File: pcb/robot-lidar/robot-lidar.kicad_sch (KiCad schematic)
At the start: 50 parts, among them J10 Conn_01x18, J2 YLIDAR X4, J3 Jack-DC, J5 Conn_01x02, J5 Conn_02x03_Odd_Even, J6 Conn_01x02, J7 Conn_01x02, J7 Conn_ARM_SWD_TagConnect_TC2030, J8 Conn_01x02, J9 Conn_01x18, SW1 SW_SPST, U1 STM32F429VETx, U2 LM317-3.3_SOT-223, U2 MPU-6050, U4 MX1508, U5 MX1508, Y1 Crystal

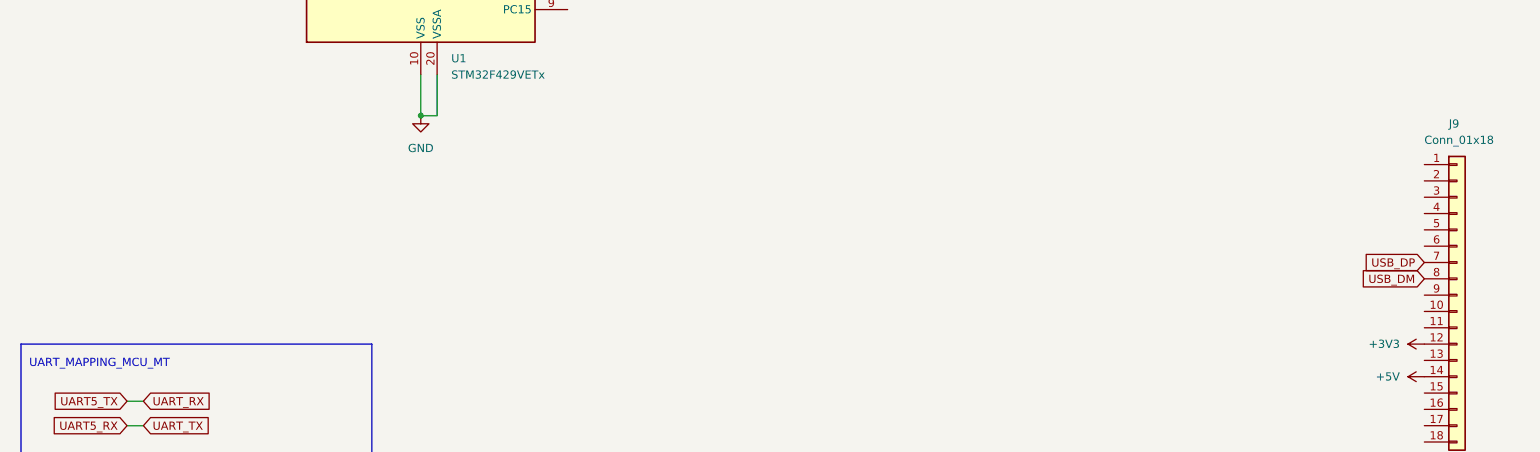
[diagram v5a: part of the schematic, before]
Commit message: add usb a connector
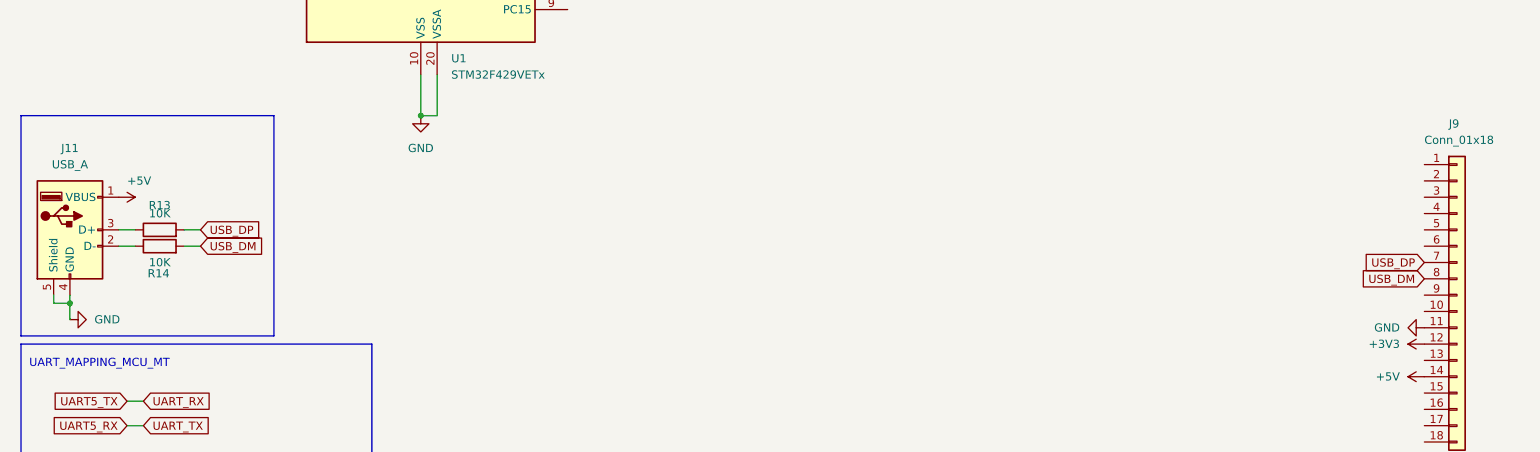
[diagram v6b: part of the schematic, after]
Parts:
- added J11: USB_A, symbol Connector:USB_A
- added R13, R14: 10K, Resistor_SMD:R_0603_1608Metric, symbol Device:R
- J10, J9: footprint (none) -> Connector_PinHeader_2.54mm:PinHeader_1x18_P2.54mm_Vertical
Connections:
- net +5V: now also J11.1 (VBUS)
- net GND: now also J9.11 (Pin_11), J11.4 (GND), J11.5 (Shield)
- net USB_DM: now also R14.2
- net USB_DP: now also R13.2
- new net: J11.3 (D+), R13.1
- new net: J11.2 (D-), R14.1
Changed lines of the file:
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@@
   (junction (at 246.38 106.68) (diameter 0) (color 0 0 0 0)
   )
+  (junction (at 22.86 219.71) (diameter 0) (color 0 0 0 0)
+  )
   (junction (at 246.38 59.69) (diameter 0) (color 0 0 0 0)
   )
@@
     (stroke (width 0) (type default))
   )
+  (wire (pts (xy 22.86 219.71) (xy 22.86 222.25))
+    (stroke (width 0) (type default))
+  )
   (wire (pts (xy 124.46 144.78) (xy 121.92 144.78))
     (stroke (width 0) (type default))
@@
     (stroke (width 0) (type default))
   )
+  (wire (pts (xy 30.48 208.28) (xy 33.02 208.28))
+    (stroke (width 0) (type default))
+  )
   (wire (pts (xy 265.43 151.13) (xy 265.43 157.48))
     (stroke (width 0) (type default))
@@
     (stroke (width 0) (type default))
   )
+  (wire (pts (xy 22.86 218.44) (xy 22.86 219.71))
+    (stroke (width 0) (type default))
+  )
   (wire (pts (xy 80.01 21.59) (xy 80.01 41.91))
     (stroke (width 0) (type default))
@@
     (stroke (width 0) (type default))
   )
+  (wire (pts (xy 40.64 208.28) (xy 43.18 208.28))
+    (stroke (width 0) (type default))
+  )
   (wire (pts (xy 121.92 138.43) (xy 121.92 144.78))
     (stroke (width 0) (type default))
@@
     (stroke (width 0) (type default))
   )
+  (wire (pts (xy 40.64 210.82) (xy 43.18 210.82))
+    (stroke (width 0) (type default))
+  )
   (wire (pts (xy 248.92 46.99) (xy 248.92 50.8))
     (stroke (width 0) (type default))
@@
     (stroke (width 0) (type default))
   )
+  (wire (pts (xy 20.32 219.71) (xy 22.86 219.71))
+    (stroke (width 0) (type default))
+  )
   (wire (pts (xy 35.56 33.02) (xy 43.18 33.02))
     (stroke (width 0) (type default))
@@
     (stroke (width 0) (type default))
   )
+  (wire (pts (xy 20.32 218.44) (xy 20.32 219.71))
+    (stroke (width 0) (type default))
+  )
   (polyline (pts (xy 321.31 41.91) (xy 358.14 41.91))
     (stroke (width 0) (type default))
@@
     (stroke (width 0) (type default))
   )
+  (wire (pts (xy 30.48 210.82) (xy 33.02 210.82))
+    (stroke (width 0) (type default))
+  )
   (wire (pts (xy 392.43 133.35) (xy 392.43 137.16))
     (stroke (width 0) (type default))
@@
     (stroke (width 0) (type default))
   )
+  (rectangle (start 15.24 190.5) (end 54.61 224.79)
+    (stroke (width 0) (type default))
+    (fill (type none))
+  )
   (rectangle (start 72.39 247.65) (end 132.08 280.67)
     (stroke (width 0) (type default))
@@
     )
   )
+  (global_label "USB_DM" (shape input) (at 43.18 210.82 0) (fields_autoplaced)
+    (effects (font (size 1.27 1.27)) (justify left))
+    (property "Intersheetrefs" "${INTERSHEET_REFS}" (at 53.6642 210.82 0)
+      (effects (font (size 1.27 1.27)) (justify left) hide)
+    )
+  )
   (global_label "M_EN" (shape input) (at 382.27 38.1 180) (fields_autoplaced)
     (effects (font (size 1.27 1.27)) (justify right))
@@
     )
   )
+  (global_label "USB_DP" (shape input) (at 43.18 208.28 0) (fields_autoplaced)
+    (effects (font (size 1.27 1.27)) (justify left))
+    (property "Intersheetrefs" "${INTERSHEET_REFS}" (at 53.4828 208.28 0)
+      (effects (font (size 1.27 1.27)) (justify left) hide)
+    )
+  )
   (global_label "MOTOR_1_B" (shape input) (at 100.33 128.27 0) (fields_autoplaced)
     (effects (font (size 1.27 1.27)) (justify left))
@@
       (effects (font (size 1.27 1.27)))
     )
-    (property "Footprint" "" (at 262.89 220.98 0)
+    (property "Footprint" "Connector_PinHeader_2.54mm:PinHeader_1x18_P2.54mm_Vertical" (at 262.89 220.98 0)
       (effects (font (size 1.27 1.27)) hide)
     )
@@
     )
   )
+  (symbol (lib_id "power:+5V") (at 30.48 203.2 270) (unit 1)
+    (in_bom yes) (on_board yes) (dnp no)
+    (property "Reference" "#PWR037" (at 26.67 203.2 0)
+      (effects (font (size 1.27 1.27)) hide)
+    )
+    (property "Value" "+5V" (at 31.75 200.66 90)
+      (effects (font (size 1.27 1.27)) (justify left))
+    )
+    (property "Footprint" "" (at 30.48 203.2 0)
+      (effects (font (size 1.27 1.27)) hide)
+    )
+    (property "Datasheet" "" (at 30.48 203.2 0)
+      (effects (font (size 1.27 1.27)) hide)
+    )
+    (pin "1")
+    (instances
+      (project "robot-lidar"
+        (path "/cb10bbf7-c2c1-4a0d-8947-ad707931d83b"
+          (reference "#PWR037") (unit 1)
+        )
+      )
+    )
+  )
   (symbol (lib_id "Device:C") (at 35.56 26.67 0) (unit 1)
     (in_bom yes) (on_board yes) (dnp no)
@@
     )
   )
+  (symbol (lib_id "Device:R") (at 36.83 208.28 90) (unit 1)
+    (in_bom yes) (on_board yes) (dnp no)
+    (property "Reference" "R13" (at 36.83 204.47 90)
+      (effects (font (size 1.27 1.27)))
+    )
+    (property "Value" "10K" (at 36.83 205.74 90)
+      (effects (font (size 1.27 1.27)))
+    )
+    (property "Footprint" "Resistor_SMD:R_0603_1608Metric" (at 36.83 210.058 90)
+      (effects (font (size 1.27 1.27)) hide)
+    )
+    (property "Datasheet" "~" (at 36.83 208.28 0)
+      (effects (font (size 1.27 1.27)) hide)
+    )
+    (pin "1")
+    (pin "2")
+    (instances
+      (project "robot-lidar"
+        (path "/cb10bbf7-c2c1-4a0d-8947-ad707931d83b"
+          (reference "R13") (unit 1)
+        )
+      )
+      (project "servo_control"
+        (path "/dcee87eb-58b7-46fe-9143-b216c98d2b37"
+          (reference "R15") (unit 1)
+        )
+      )
+    )
+  )
   (symbol (lib_id "Device:C") (at 66.04 26.67 0) (unit 1)
     (in_bom yes) (on_board yes) (dnp no)
@@
     )
   )
+  (symbol (lib_id "power:GND") (at 233.68 223.52 270) (unit 1)
+    (in_bom yes) (on_board yes) (dnp no) (fields_autoplaced)
+    (property "Reference" "#PWR036" (at 227.33 223.52 0)
+      (effects (font (size 1.27 1.27)) hide)
+    )
+    (property "Value" "GND" (at 229.87 223.52 90)
+      (effects (font (size 1.27 1.27)) (justify right))
+    )
+    (property "Footprint" "" (at 233.68 223.52 0)
+      (effects (font (size 1.27 1.27)) hide)
+    )
+    (property "Datasheet" "" (at 233.68 223.52 0)
+      (effects (font (size 1.27 1.27)) hide)
+    )
+    (pin "1")
+    (instances
+      (project "robot-lidar"
+        (path "/cb10bbf7-c2c1-4a0d-8947-ad707931d83b"
+          (reference "#PWR036") (unit 1)
+        )
+      )
+    )
+  )
   (symbol (lib_id "Device:C") (at 392.43 67.31 0) (unit 1)
     (in_bom yes) (on_board yes) (dnp no)
@@
     )
   )
+  (symbol (lib_id "Connector:USB_A") (at 22.86 208.28 0) (unit 1)
+    (in_bom yes) (on_board yes) (dnp no) (fields_autoplaced)
+    (property "Reference" "J11" (at 22.86 195.58 0)
+      (effects (font (size 1.27 1.27)))
+    )
+    (property "Value" "USB_A" (at 22.86 198.12 0)
+      (effects (font (size 1.27 1.27)))
+    )
+    (property "Footprint" "" (at 26.67 209.55 0)
+      (effects (font (size 1.27 1.27)) hide)
+    )
+    (property "Datasheet" " ~" (at 26.67 209.55 0)
+      (effects (font (size 1.27 1.27)) hide)
+    )
+    (pin "1")
+    (pin "2")
+    (pin "3")
+    (pin "4")
+    (pin "5")
+    (instances
+      (project "robot-lidar"
+        (path "/cb10bbf7-c2c1-4a0d-8947-ad707931d83b"
+          (reference "J11") (unit 1)
+        )
+      )
+    )
+  )
   (symbol (lib_id "Device:C_Polarized_Small") (at 265.43 68.58 0) (unit 1)
     (in_bom yes) (on_board yes) (dnp no)
@@
       (effects (font (size 1.27 1.27)) (justify left))
     )
-    (property "Footprint" "" (at 238.76 218.44 0)
+    (property "Footprint" "Connector_PinHeader_2.54mm:PinHeader_1x18_P2.54mm_Vertical" (at 238.76 218.44 0)
       (effects (font (size 1.27 1.27)) hide)
     )
@@
     )
   )
+  (symbol (lib_id "Device:R") (at 36.83 210.82 90) (unit 1)
+    (in_bom yes) (on_board yes) (dnp no)
+    (property "Reference" "R14" (at 36.6545 215.08 90)
+      (effects (font (size 1.27 1.27)))
+    )
+    (property "Value" "10K" (at 36.83 213.36 90)
+      (effects (font (size 1.27 1.27)))
+    )
+    (property "Footprint" "Resistor_SMD:R_0603_1608Metric" (at 36.83 212.598 90)
+      (effects (font (size 1.27 1.27)) hide)
+    )
+    (property "Datasheet" "~" (at 36.83 210.82 0)
+      (effects (font (size 1.27 1.27)) hide)
+    )
+    (pin "1")
+    (pin "2")
+    (instances
+      (project "robot-lidar"
+        (path "/cb10bbf7-c2c1-4a0d-8947-ad707931d83b"
+          (reference "R14") (unit 1)
+        )
+      )
+      (project "servo_control"
+        (path "/dcee87eb-58b7-46fe-9143-b216c98d2b37"
+          (reference "R15") (unit 1)
+        )
+      )
+    )
+  )
   (symbol (lib_id "power:+5V") (at 270.51 139.7 270) (unit 1)
     (in_bom yes) (on_board yes) (dnp no) (fields_autoplaced)
@@
         )
       )
+    )
+  )
+  (symbol (lib_id "power:GND") (at 22.86 222.25 90) (unit 1)
+    (in_bom yes) (on_board yes) (dnp no) (fields_autoplaced)
+    (property "Reference" "#PWR038" (at 29.21 222.25 0)
+      (effects (font (size 1.27 1.27)) hide)
+    )
+    (property "Value" "GND" (at 26.67 222.25 90)
+      (effects (font (size 1.27 1.27)) (justify right))
+    )
+    (property "Footprint" "" (at 22.86 222.25 0)
+      (effects (font (size 1.27 1.27)) hide)
+    )
+    (property "Datasheet" "" (at 22.86 222.25 0)
+      (effects (font (size 1.27 1.27)) hide)
+    )
+    (pin "1")
+    (instances
+      (project "robot-lidar"
+        (path "/cb10bbf7-c2c1-4a0d-8947-ad707931d83b"
+          (reference "#PWR038") (unit 1)
+        )
+      )

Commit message: add usb connector on pcb
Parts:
- J11: footprint (none) -> Connector_USB:USB_A_Molex_48037-2200_Horizontal
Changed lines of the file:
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@@
       (effects (font (size 1.27 1.27)))
     )
-    (property "Footprint" "" (at 26.67 209.55 0)
+    (property "Footprint" "Connector_USB:USB_A_Molex_48037-2200_Horizontal" (at 26.67 209.55 0)
       (effects (font (size 1.27 1.27)) hide)
     )
